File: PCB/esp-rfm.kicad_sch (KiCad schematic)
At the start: 39 parts, among them IC1 RFM69_9X, J3 Conn_Coaxial, J4 USB_C_Receptacle_USB2.0, J5 Conn_01x04, J6 Conn_01x03, Q1 BC847, Q2 BC847, SW1 RST/CONFIG, U1 ESP-12F, U2 AMS1117-3.3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

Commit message: add radio applications cleanup
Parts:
- added U4: USBLC6-2SC6, Package_TO_SOT_SMD:SOT-23-6, symbol Power_Protection:USBLC6-2SC6
- Brd1, IC1, J3, JP1, JP2: now not fitted
- C1, C2, C4: LCSC (none) -> C319192; LCSC order # C319192 -> (none)
- C5: LCSC (none) -> C15850; LCSC order # C15850 -> (none)
- C5, C8: LCSC (none) -> C59937; LCSC order # C59937 -> (none)
- C6, C7: LCSC (none) -> C344180; LCSC order # C344180 -> (none)
- D2: LCSC (none) -> C57759; LCSC order # C57759 -> (none)
- J4: LCSC (none) -> C2927037; LCSC order # C2927037 -> (none)
- J5: LCSC (none) -> C5116483
- J6: LCSC (none) -> C49257
- Q1, Q2: LCSC (none) -> C181141; LCSC order # C181141 -> (none)
- R1, R2: LCSC (none) -> C431925; LCSC order # C431925 -> (none)
- R10: LCSC (none) -> C17633; LCSC order # C17633 -> (none)
- R10, R11, R3, R4, R8, R9: LCSC (none) -> C114531; LCSC order # C114531 -> (none)
- R12, R13, R5, R6, R8: LCSC (none) -> C110775; LCSC order # C110775 -> (none)
- SW1: LCSC (none) -> C2837540; LCSC order # C2837540 -> (none)
- U1: LCSC (none) -> C82891; LCSC order # C82891 -> (none)
- U2: LCSC (none) -> C351784; LCSC order # C351784 -> (none)
- U3: LCSC (none) -> C84681; LCSC order # C84681 -> (none)
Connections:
- net +5V: now also U4.5 (VBUS)
- net GND: now also U4.2 (GND)
- net at J4.A6 (D+), J4.B6 (D+): now also U4.1 (I/O1); no longer U3.5 (UD+)
- net at J4.A7 (D-), J4.B7 (D-): now also U4.3 (I/O2); no longer U3.6 (UD-)
- new net: U3.6 (UD-), U4.4 (I/O2)
- new net: U3.5 (UD+), U4.6 (I/O1)
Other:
- moved on the sheet: C1, C2, C6, C7, Q1, Q2, R1, R12, R13, R2, U2, U3

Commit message: fix warning in platformio.ini
status LED blinker
update PCB
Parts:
- H1, H2: now left out of the parts list
- IC1, J3, JP1, JP2: now fitted; now left out of the parts list
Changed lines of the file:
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@@
 		(unit 1)
 		(exclude_from_sim no)
-		(in_bom yes)
+		(in_bom no)
 		(on_board yes)
-		(dnp yes)
+		(dnp no)
 		(fields_autoplaced yes)
 		(property "Reference" "JP2"
@@
 		(unit 1)
 		(exclude_from_sim no)
-		(in_bom yes)
+		(in_bom no)
 		(on_board yes)
 		(dnp no)
@@
 		(unit 1)
 		(exclude_from_sim no)
-		(in_bom yes)
+		(in_bom no)
 		(on_board yes)
 		(dnp no)
@@
 		(unit 1)
 		(exclude_from_sim no)
-		(in_bom yes)
+		(in_bom no)
 		(on_board yes)
-		(dnp yes)
+		(dnp no)
 		(property "Reference" "IC1"
 			(at 228.6 121.92 0)
@@
 		(unit 1)
 		(exclude_from_sim no)
-		(in_bom yes)
+		(in_bom no)
 		(on_board yes)
-		(dnp yes)
+		(dnp no)
 		(fields_autoplaced yes)
 		(property "Reference" "JP1"
@@
 		(unit 1)
 		(exclude_from_sim no)
-		(in_bom yes)
+		(in_bom no)
 		(on_board yes)
-		(dnp yes)
+		(dnp no)
 		(fields_autoplaced yes)
 		(property "Reference" "J3"

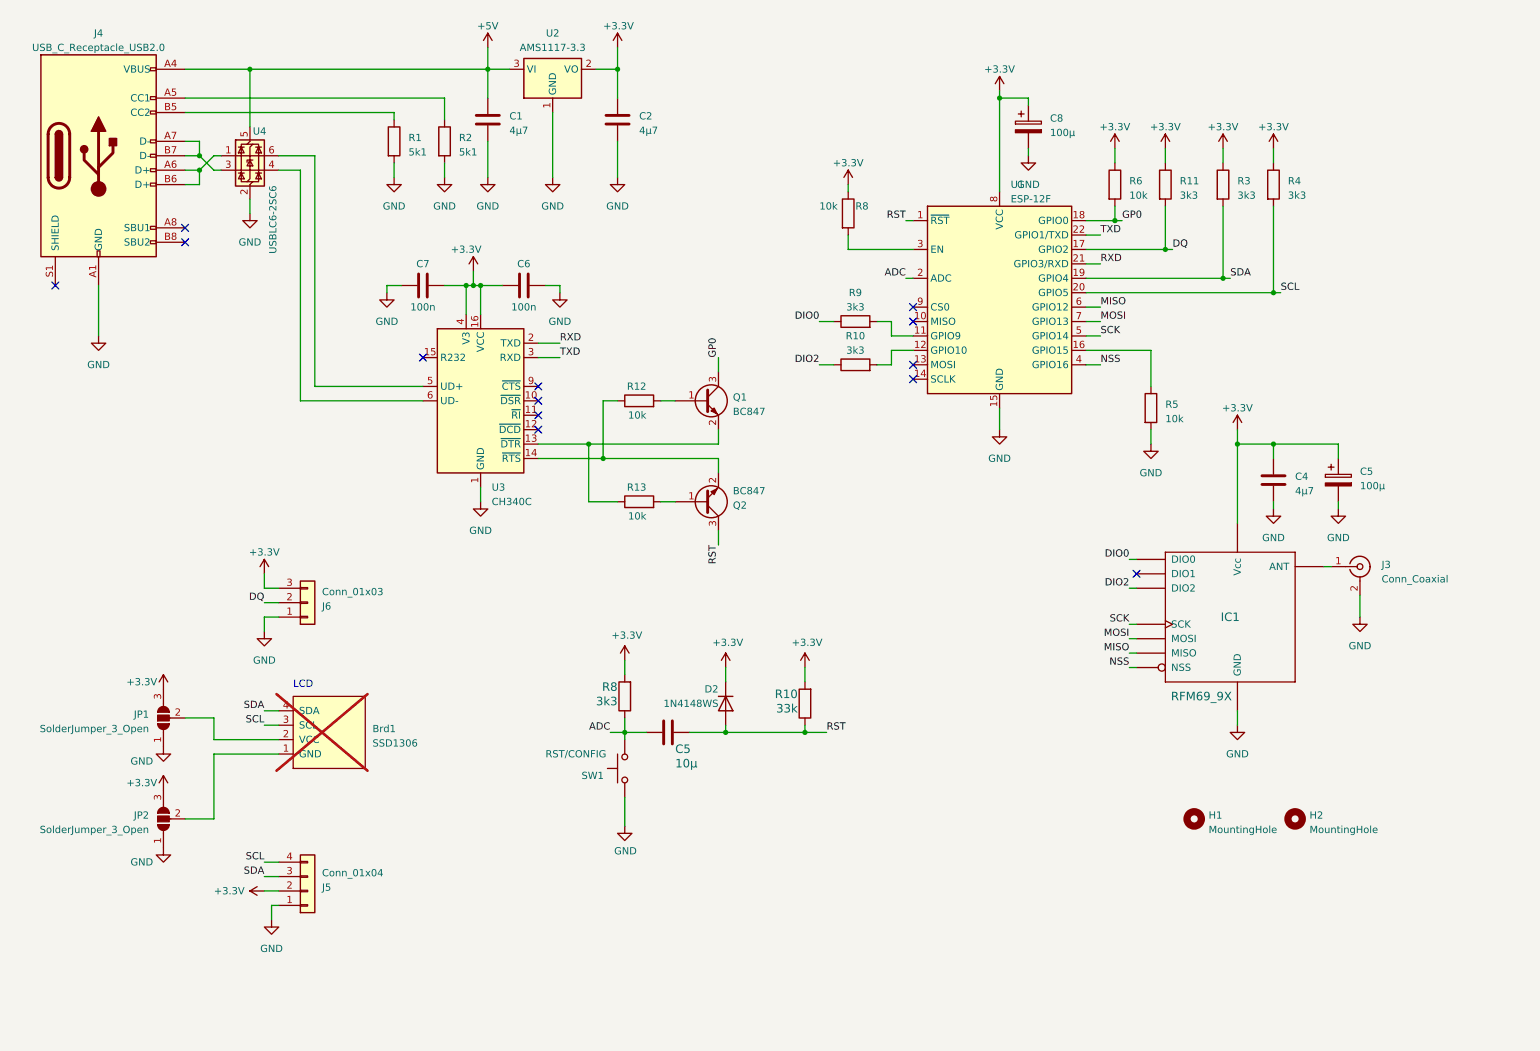
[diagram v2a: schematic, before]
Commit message: change pin header add ferrite
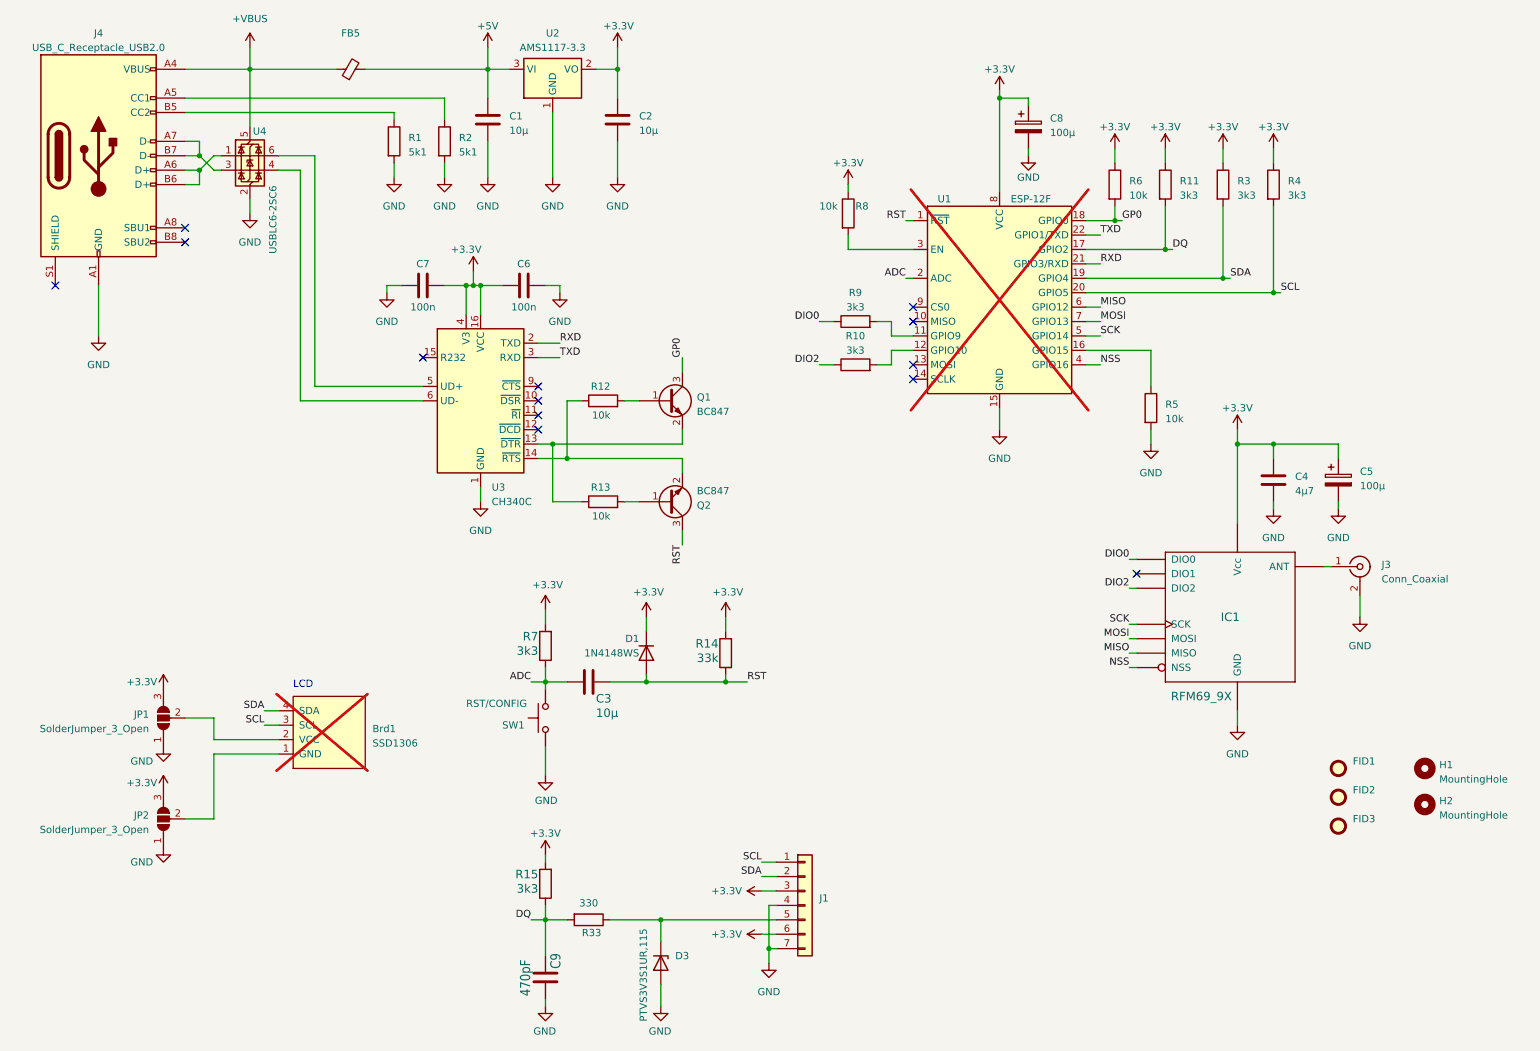
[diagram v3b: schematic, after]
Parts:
- removed J5: Conn_01x04, Connector_PinHeader_2.54mm:PinHeader_1x04_P2.54mm_Vertical, symbol Connector_Generic:Conn_01x04
- removed J6: Conn_01x03, Connector_PinHeader_2.54mm:PinHeader_1x03_P2.54mm_Vertical, symbol Connector_Generic:Conn_01x03
- added C9: 470pF, Capacitor_SMD:C_0805_2012Metric, symbol Device:C
- added D3: PTVS3V3S1UR,115, Diode_SMD:D_SOD-123, symbol Device:D_Zener
- added FB5: ~, Inductor_SMD:L_0603_1608Metric, symbol Device:FerriteBead_Small
- added FID1, FID2, FID3: ~, Fiducial:Fiducial_1mm_Mask2mm, symbol Mechanical:Fiducial
- added J1: ~, Connector_PinHeader_2.54mm:PinHeader_1x07_P2.54mm_Vertical, symbol Connector_Generic:Conn_01x07
- added R15: 3k3, Resistor_SMD:R_0805_2012Metric, symbol Device:R
- added R33: 330, Resistor_SMD:R_0805_2012Metric, symbol Device:R
- C1, C2: value 4µ7 -> 10µ; LCSC C319192 -> C90543
- R10, R11, R3, R4, R9: LCSC C114531 -> C26010
- R7: renamed from R8; LCSC C114531 -> C26010
- U1: now not fitted; now left out of the parts list
- U4: LCSC (none) -> C2827654
- renumbered C5 to C3, D2 to D1, R10 to R14
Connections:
- net +3.3V: now also J1.3 (Pin_3), J1.6 (Pin_6), R15.2
- net +5V: now also FB5.2; no longer J4.A4 (VBUS), J4.A9 (VBUS), J4.B4 (VBUS), J4.B9 (VBUS), U4.5 (VBUS)
- net DQ: now also C9.1, R15.1, R33.2
- net GND: now also C9.2, D3.2 (A), J1.4 (Pin_4), J1.7 (Pin_7)
- net SCL: now also J1.1 (Pin_1)
- net SDA: now also J1.2 (Pin_2)
- new net: D3.1 (K), J1.5 (Pin_5), R33.1
- new net +VBUS: FB5.1, J4.A4 (VBUS), J4.A9 (VBUS), J4.B4 (VBUS), J4.B9 (VBUS), U4.5 (VBUS)
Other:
- moved on the sheet: C3, D1, H1, H2, Q1, Q2, R12, R13, R14, R7, SW1
